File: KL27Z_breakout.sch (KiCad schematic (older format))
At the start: 15 parts, among them J1 USB_mini_micro_B, P1 CONN_01X08, P2 CONN_01X08, P3 CONN_01X08, P4 CONN_01X08, SW1 SW_PUSH, SW2 SW_PUSH, U1 MKL27Z256VFM4

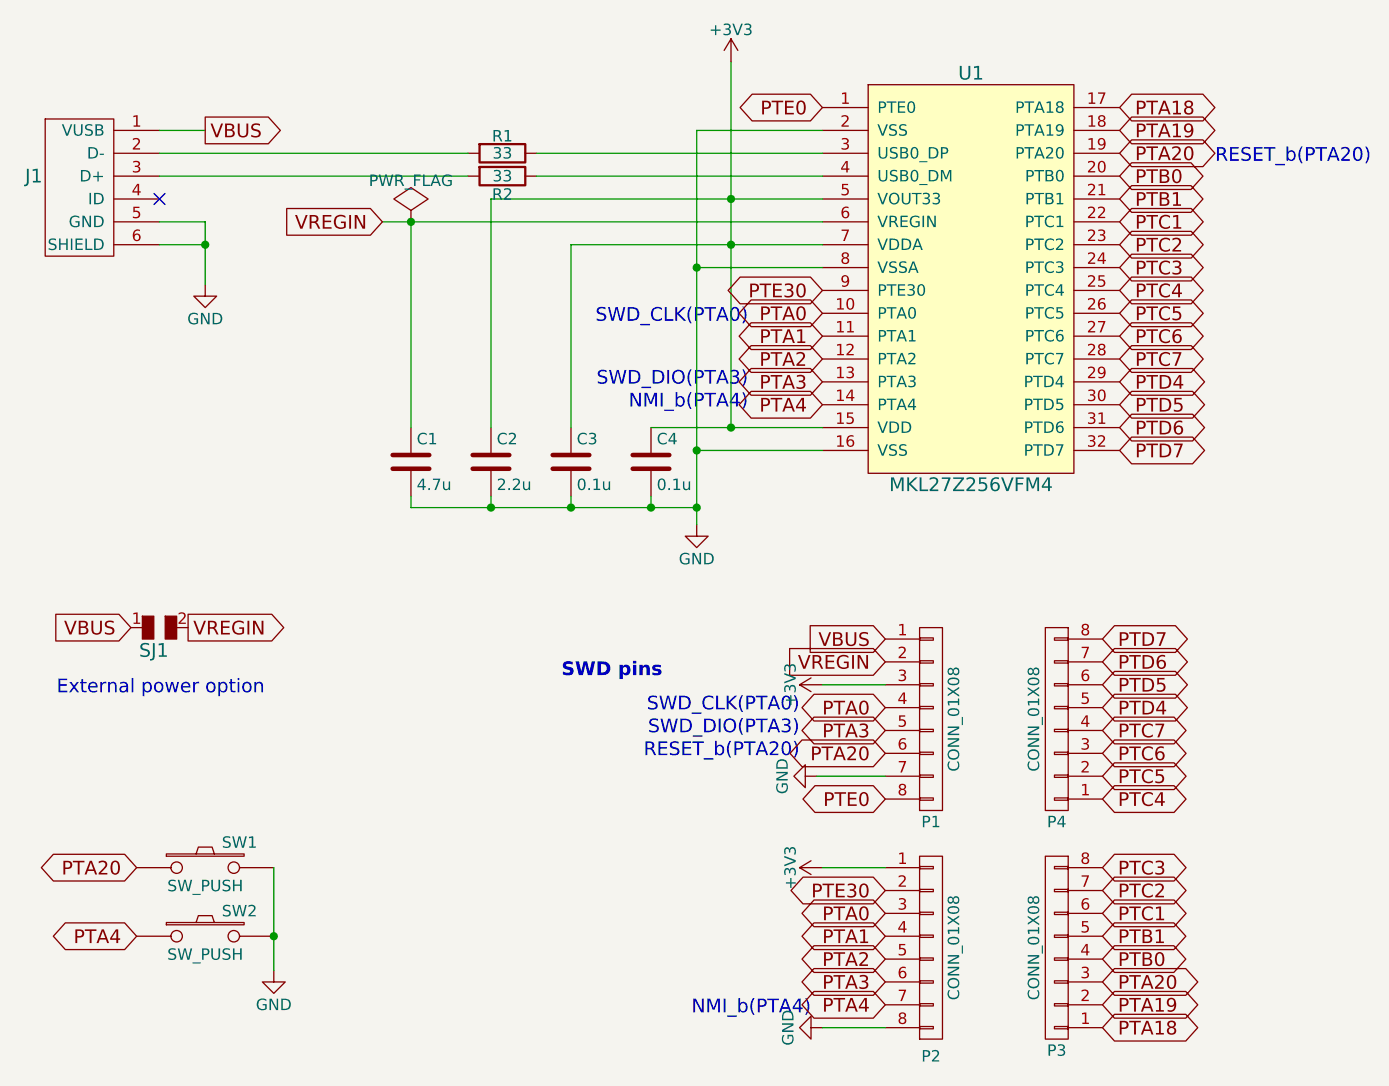
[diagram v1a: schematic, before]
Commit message: Fix D- and D+ lines and pin header position
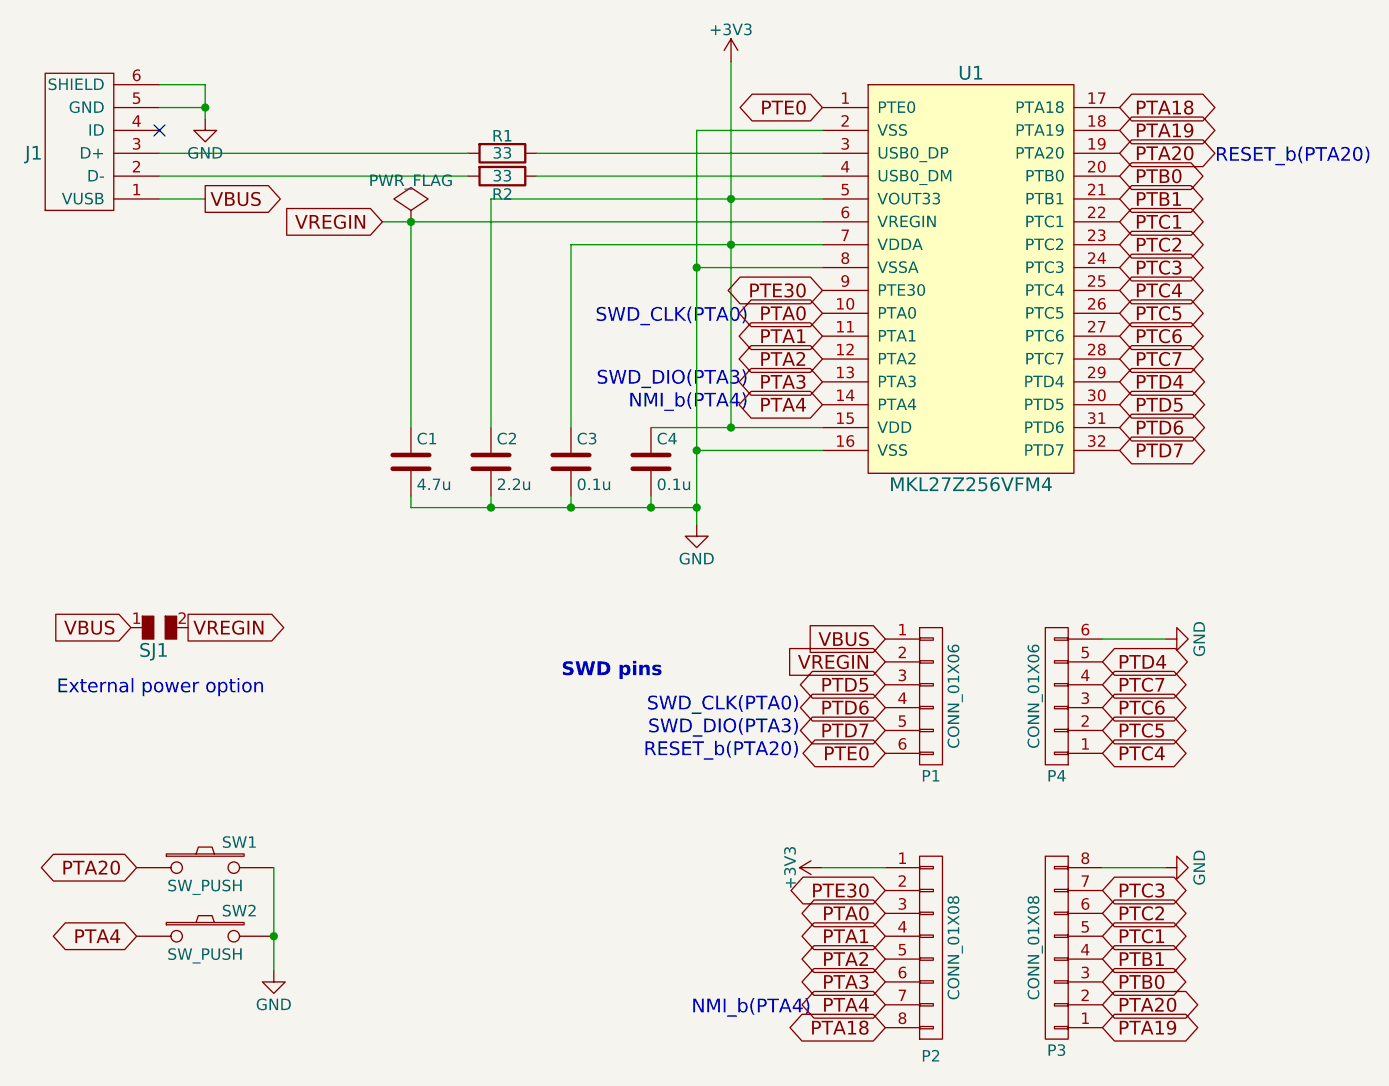
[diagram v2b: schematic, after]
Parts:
- removed P1, P4: CONN_01X08, symbol CONN_01X08
- added P1, P4: CONN_01X06, symbol CONN_01X06
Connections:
- net GND: now also P3.8 (P8), P4.6 (P6); no longer P2.8 (P8)
- net PTA18: now also P2.8 (P8); no longer P3.1 (P1)
- net PTA19: now also P3.1 (P1); no longer P3.2 (P2)
- net PTA20: now also P3.2 (P2); no longer P3.3 (P3)
- net PTB0: now also P3.3 (P3); no longer P3.4 (P4)
- net PTB1: now also P3.4 (P4); no longer P3.5 (P5)
- net PTC1: now also P3.5 (P5); no longer P3.6 (P6)
- net PTC2: now also P3.6 (P6); no longer P3.7 (P7)
- net PTC3: now also P3.7 (P7); no longer P3.8 (P8)
- net PTC4: now also P4.1 (P1)
- net PTC5: now also P4.2 (P2)
- net PTC6: now also P4.3 (P3)
- net PTC7: now also P4.4 (P4)
- net PTD4: now also P4.5 (P5)
- net PTD5: now also P1.3 (P3)
- net PTD6: now also P1.4 (P4)
- net PTD7: now also P1.5 (P5)
- net PTE0: now also P1.6 (P6)
- net VBUS: now also P1.1 (P1)
- net VREGIN: now also P1.2 (P2)
- net at J1.2 (D-): now also R2.2; no longer R1.2
- net at J1.3 (D+): now also R1.2; no longer R2.2
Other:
- moved on the sheet: J1
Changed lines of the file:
@@
 EESchema Schematic File Version 2
+LIBS:KL27Z_breakout-rescue
 LIBS:power
 LIBS:device
@@
 LIBS:mkl27z256vfm4
 LIBS:keyboard_parts
+LIBS:KL27Z_breakout-cache
 EELAYER 25 0
 EELAYER END
@@
 F 3 "" H 1650 1850 60  0000 C CNN
 	1    1700 1850
-	1    0    0    -1
-$EndComp
-NoConn ~ 1850 2000
+	1    0    0    1
+$EndComp
+NoConn ~ 1850 1700
 $Comp
 L GND #PWR01
 U 1 1 57578F62
-P 2050 2375
-F 0 "#PWR01" H 2050 2125 50  0001 C CNN
-F 1 "GND" H 2050 2225 50  0000 C CNN
-F 2 "" H 2050 2375 50  0000 C CNN
-F 3 "" H 2050 2375 50  0000 C CNN
-	1    2050 2375
+P 2050 1650
+F 0 "#PWR01" H 2050 1400 50  0001 C CNN
+F 1 "GND" H 2050 1500 50  0000 C CNN
+F 2 "" H 2050 1650 50  0000 C CNN
+F 3 "" H 2050 1650 50  0000 C CNN
+	1    2050 1650
 	1    0    0    -1
 $EndComp
@@
 Text GLabel 2825 2100 0    60   Input ~ 0
 VREGIN
-Text GLabel 2050 1700 2    60   Output ~ 0
+Text GLabel 2050 2000 2    60   Output ~ 0
 VBUS
 $Comp
@@
 	1    0    0    -1
 $EndComp
-$Comp
-L CONN_01X08 P4
-U 1 1 5757D546
-P 5775 4275
-F 0 "P4" H 5775 4725 50  0000 C CNN
-F 1 "CONN_01X08" V 5875 4275 50  0000 C CNN
-F 2 "" H 5775 4275 50  0001 C CNN
-F 3 "" H 5775 4275 50  0000 C CNN
-	1    5775 4275
-	-1   0    0    1
-$EndComp
-$Comp
-L CONN_01X08 P1
-U 1 1 5757D54C
-P 5225 4275
-F 0 "P1" H 5225 3825 50  0000 C CNN
-F 1 "CONN_01X08" V 5325 4275 50  0000 C CNN
-F 2 "" H 5225 4275 50  0001 C CNN
-F 3 "" H 5225 4275 50  0000 C CNN
-	1    5225 4275
-	1    0    0    -1
-$EndComp
 Text Notes 4650 4350 2    60   ~ 0
 SWD_DIO(PTA3)
 Text GLabel 5025 3925 0    60   Input ~ 0
 VBUS
-$Comp
-L +3V3 #PWR04
-U 1 1 5757ECBC
-P 4750 4125
-F 0 "#PWR04" H 4750 3975 50  0001 C CNN
-F 1 "+3V3" H 4750 4265 50  0000 C CNN
-F 2 "" H 4750 4125 50  0000 C CNN
-F 3 "" H 4750 4125 50  0000 C CNN
-	1    4750 4125
-	0    -1   -1   0
-$EndComp
-Text GLabel 5975 3925 2    60   BiDi ~ 0
+Text GLabel 5025 4325 0    60   BiDi ~ 0
 PTD7
+Text GLabel 5025 4225 0    60   BiDi ~ 0
+PTD6
 Text GLabel 5975 4025 2    60   BiDi ~ 0
-PTD6
+PTD4
+Text GLabel 5975 4125 2    60   BiDi ~ 0
+PTC7
 Text GLabel 5975 4225 2    60   BiDi ~ 0
-PTD4
+PTC6
 Text GLabel 5975 4325 2    60   BiDi ~ 0
-PTC7
+PTC5
 Text GLabel 5975 4425 2    60   BiDi ~ 0
-PTC6
-Text GLabel 5975 4525 2    60   BiDi ~ 0
-PTC5
-Text GLabel 5975 4625 2    60   BiDi ~ 0
 PTC4
-Text GLabel 5975 4925 2    60   BiDi ~ 0
+Text GLabel 5975 5025 2    60   BiDi ~ 0
 PTC3
-Text GLabel 5975 5025 2    60   BiDi ~ 0
+Text GLabel 5975 5125 2    60   BiDi ~ 0
 PTC2
-Text GLabel 5975 5125 2    60   BiDi ~ 0
+Text GLabel 5975 5225 2    60   BiDi ~ 0
 PTC1
-Text GLabel 5975 5225 2    60   BiDi ~ 0
+Text GLabel 5975 5325 2    60   BiDi ~ 0
 PTB1
-Text GLabel 5975 5325 2    60   BiDi ~ 0
+Text GLabel 5975 5425 2    60   BiDi ~ 0
 PTB0
-Text GLabel 5975 5425 2    60   BiDi ~ 0
+Text GLabel 5975 5525 2    60   BiDi ~ 0
 PTA20
-Text GLabel 5975 5525 2    60   BiDi ~ 0
+Text GLabel 5975 5625 2    60   BiDi ~ 0
 PTA19
-Text GLabel 5975 5625 2    60   BiDi ~ 0
+Text GLabel 5025 5625 0    60   BiDi ~ 0
 PTA18
 Text Notes 4650 4450 2    60   ~ 0
@@
 Text GLabel 5025 4025 0    60   Input ~ 0
 VREGIN
-Text GLabel 5025 4625 0    60   BiDi ~ 0
+Text GLabel 5025 4425 0    60   BiDi ~ 0
 PTE0
 $Comp
@@
 Text GLabel 1750 5225 0    60   BiDi ~ 0
 PTA4
-Text GLabel 5025 4225 0    60   BiDi ~ 0
-PTA0
-Text GLabel 5025 4325 0    60   BiDi ~ 0
-PTA3
-Text GLabel 5025 4425 0    60   BiDi ~ 0
-PTA20
-$Comp
-L GND #PWR06
-U 1 1 57582552
-P 4725 4525
-F 0 "#PWR06" H 4725 4275 50  0001 C CNN
-F 1 "GND" H 4725 4375 50  0000 C CNN
-F 2 "" H 4725 4525 50  0000 C CNN
-F 3 "" H 4725 4525 50  0000 C CNN
-	1    4725 4525
-	0    1    1    0
-$EndComp
 Text Notes 4650 4250 2    60   ~ 0
 SWD_CLK(PTA0)
-$Comp
-L GND #PWR07
-U 1 1 5758372E
-P 4750 5625
-F 0 "#PWR07" H 4750 5375 50  0001 C CNN
-F 1 "GND" H 4750 5475 50  0000 C CNN
-F 2 "" H 4750 5625 50  0000 C CNN
-F 3 "" H 4750 5625 50  0000 C CNN
-	1    4750 5625
-	0    1    1    0
-$EndComp
 Text Notes 4700 5575 2    60   ~ 0
 NMI_b(PTA4)
@@
 	1    0    0    -1
 $EndComp
+Text GLabel 5025 4125 0    60   BiDi ~ 0
+PTD5
+Wire Wire Line
+	2050 1500 2050 1650
+Wire Wire Line
+	5025 4925 4750 4925
+Connection ~ 2350 5225
+Wire Wire Line
+	2350 4925 2350 5375
+Wire Wire Line
+	3300 2000 3300 3000
+Connection ~ 3300 3350
+Wire Wire Line
+	2950 3300 2950 3350
+Connection ~ 2950 2100
+Wire Wire Line
+	2950 3000 2950 2100
+Wire Wire Line
+	3650 3300 3650 3350
+Connection ~ 4000 3350
+Connection ~ 4200 3350
+Wire Wire Line
+	3650 2200 3650 3000
+Connection ~ 4200 2300
+Wire Wire Line
+	4750 1700 4200 1700
+Connection ~ 4200 3100
+Wire Wire Line
+	4750 2300 4200 2300
+Wire Wire Line
+	4200 1700 4200 3425
+Wire Wire Line
+	4750 3100 4200 3100
+Connection ~ 4350 3000
+Connection ~ 4350 2000
+Connection ~ 4350 2200
+Wire Wire Line
+	4350 1400 4350 3000
+Wire Wire Line
+	3300 2000 4750 2000
+Connection ~ 3650 3350
+Wire Wire Line
+	2950 3350 4200 3350
+Wire Wire Line
+	4000 3300 4000 3350
+Wire Wire Line
+	4750 3000 4000 3000
+Wire Wire Line
+	4750 2200 3650 2200
+Wire Wire Line
+	3300 3300 3300 3350
+Wire Wire Line
+	1850 2000 2050 2000
+Connection ~ 2050 1600
+Wire Wire Line
+	1850 1600 2050 1600
+Wire Wire Line
+	1850 1500 2050 1500
+Wire Wire Line
+	1850 1900 3200 1900
+Wire Wire Line
+	1850 1800 3200 1800
+Wire Wire Line
+	2825 2100 4750 2100
+Wire Wire Line
+	3500 1900 4750 1900
 Wire Wire Line
 	3500 1800 4750 1800
-Wire Wire Line
-	3500 1900 4750 1900
-Wire Wire Line
-	2825 2100 4750 2100
-Wire Wire Line
-	1850 1800 3200 1800
-Wire Wire Line
-	1850 1900 3200 1900
-Wire Wire Line
-	1850 2100 2050 2100
-Wire Wire Line
-	2050 2100 2050 2375
-Wire Wire Line
-	1850 2200 2050 2200
-Connection ~ 2050 2200
-Wire Wire Line
-	1850 1700 2050 1700
-Wire Wire Line
-	3300 3300 3300 3350
-Wire Wire Line
-	4750 2200 3650 2200
-Wire Wire Line
-	4750 3000 4000 3000
-Wire Wire Line
-	4000 3300 4000 3350
-Wire Wire Line
-	2950 3350 4200 3350
-Connection ~ 3650 3350
-Wire Wire Line
-	3300 2000 4750 2000
-Wire Wire Line
-	4350 1400 4350 3000
-Connection ~ 4350 2200
-Connection ~ 4350 2000
-Connection ~ 4350 3000
-Wire Wire Line
-	4750 3100 4200 3100
-Wire Wire Line
-	4200 1700 4200 3425
-Wire Wire Line
-	4750 2300 4200 2300
-Connection ~ 4200 3100
-Wire Wire Line
-	4750 1700 4200 1700
-Connection ~ 4200 2300
-Wire Wire Line
-	3650 2200 3650 3000
-Connection ~ 4200 3350
-Connection ~ 4000 3350
-Wire Wire Line
-	3650 3300 3650 3350
-Wire Wire Line
-	2950 3000 2950 2100
-Connection ~ 2950 2100
-Wire Wire Line
-	2950 3300 2950 3350
-Connection ~ 3300 3350
-Wire Wire Line
-	5025 4125 4750 4125
-Wire Wire Line
-	3300 2000 3300 3000
-Wire Wire Line
-	2350 4925 2350 5375
-Connection ~ 2350 5225
-Wire Wire Line
-	5025 4525 4725 4525
-Wire Wire Line
-	5025 5625 4750 5625
-Wire Wire Line
-	5025 4925 4750 4925
-Text GLabel 5975 4125 2    60   BiDi ~ 0
-PTD5
+$Comp
+L GND #PWR?
+U 1 1 579F5C7F
+P 6250 4925
+F 0 "#PWR?" H 6250 4675 50  0001 C CNN
+F 1 "GND" H 6250 4775 50  0000 C CNN
+F 2 "" H 6250 4925 50  0000 C CNN
+F 3 "" H 6250 4925 50  0000 C CNN
+	1    6250 4925
+	0    -1   -1   0
+$EndComp
+Wire Wire Line
+	6250 4925 5975 4925
+$Comp
+L GND #PWR?
+U 1 1 579F5F33
+P 6250 3925
+F 0 "#PWR?" H 6250 3675 50  0001 C CNN
+F 1 "GND" H 6250 3775 50  0000 C CNN
+F 2 "" H 6250 3925 50  0000 C CNN
+F 3 "" H 6250 3925 50  0000 C CNN
+	1    6250 3925
+	0    -1   -1   0
+$EndComp
+Wire Wire Line
+	6250 3925 5975 3925
+$Comp
+L CONN_01X06 P4
+U 1 1 579F6106
+P 5775 4175
+F 0 "P4" H 5775 4525 50  0000 C CNN
+F 1 "CONN_01X06" V 5875 4175 50  0000 C CNN
+F 2 "" H 5775 4175 50  0000 C CNN
+F 3 "" H 5775 4175 50  0000 C CNN
+	1    5775 4175
+	-1   0    0    1
+$EndComp
+$Comp
+L CONN_01X06 P1
+U 1 1 579F629B
+P 5225 4175
+F 0 "P1" H 5225 3825 50  0000 C CNN
+F 1 "CONN_01X06" V 5325 4175 50  0000 C CNN
+F 2 "" H 5225 4175 50  0000 C CNN
+F 3 "" H 5225 4175 50  0000 C CNN
+	1    5225 4175
+	1    0    0    -1
+$EndComp
 $EndSCHEMATC
